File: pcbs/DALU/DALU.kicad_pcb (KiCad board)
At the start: 4 copper layers, 51 parts, among them J201 Conn_02x20_Odd_Even, U201 74HC245, U202 74HC245, U203 74HC245, U301 74HC138, U401 74HC86, U402 74HC86, U403 74HC86, U404 74HC08, U405 74HC283, U406 74HC283, U407 74HC245, U408 74HC245, U501 74HC00, U502 74HC00, U503 74HC245, U601 74HC86, U602 74HC86, U603 74HC245, U701 74HC32, U702 74HC32, U703 74HC245, U801 74HC74, U802 74HC32, U803 74HCT574, U901 74HC08, U902 74HC08, U903 74HC245

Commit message: Fixing a lot of routing
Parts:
- added C401: 100n, Capacitor_SMD:C_0603_1608Metric, F.Cu at (74.9, 47.0)
- added C402: 100n, Capacitor_SMD:C_0603_1608Metric, F.Cu at (58.4, 72.4)
- added C403: 100n, Capacitor_SMD:C_0603_1608Metric, F.Cu at (90.2, 47.0)
- added C404: 100n, Capacitor_SMD:C_0603_1608Metric, F.Cu at (105.4, 47.0)
- added C405: 100n, Capacitor_SMD:C_0603_1608Metric, F.Cu at (73.7, 69.4)
- added C406: 100n, Capacitor_SMD:C_0603_1608Metric, F.Cu at (88.9, 69.3)
- added C501: 100n, Capacitor_SMD:C_0603_1608Metric, F.Cu at (94.0, 138.7)
- added C502: 100n, Capacitor_SMD:C_0603_1608Metric, F.Cu at (97.3, 163.8)
- added C503: 100n, Capacitor_SMD:C_0603_1608Metric, F.Cu at (111.8, 139.7)
- added C601: 100n, Capacitor_SMD:C_0603_1608Metric, F.Cu at (149.9, 47.0)
- added C602: 100n, Capacitor_SMD:C_0603_1608Metric, F.Cu at (149.9, 68.6)
- added C603: 100n, Capacitor_SMD:C_0603_1608Metric, F.Cu at (163.8, 44.5)
- moved U402 61.4 mm to (52.1, 76.2)
- moved U407 23.4 mm to (101.6, 73.7)
- moved U408 16.1 mm to (101.6, 88.9)
- moved U603 4.02 mm to (158.8, 53.3)
- moved U503 4.02 mm to (106.7, 148.6)
- moved U404 1.28 mm to (94.0, 47.0)
- moved U401 1.26 mm to (63.5, 47.0)
- moved U405 1.26 mm to (63.5, 68.6)
- moved C701 0.76 mm to (168.9, 138.7)
- moved C702 0.76 mm to (172.2, 163.8)
- moved C703 0.76 mm to (186.7, 139.7)
- moved U701 0.76 mm to (161.3, 142.2)
- moved U702 0.76 mm to (161.3, 163.8)
- moved U703 0.76 mm to (181.6, 148.6)
- renumbered U404 to U402, U402 to U404
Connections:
- U402 pad 10: unconnected-(U404-Pad10) -> +5V
- U402 pad 11: unconnected-(U404-Pad11) (its old number) -> Net-(U401-Pad10)
- U402 pad 12: unconnected-(U404-Pad12) (its old number) -> /AdderSubtractor/~{ADD}
- U402 pad 13: unconnected-(U404-Pad13) (its old number) -> +5V
- U402 pad 14: unconnected-(U404-Pad14) -> +5V
- U402 pad 7: unconnected-(U404-Pad7) -> GND
- U402 pad 8: unconnected-(U404-Pad8) -> Net-(U403-Pad10)
- U402 pad 9: unconnected-(U404-Pad9) -> /AdderSubtractor/~{ADD}
- U403 pad 10: Net-(U402-Pad6) -> Net-(U403-Pad10)
- U403 pad 13: Net-(U402-Pad6) -> Net-(U403-Pad10)
- U403 pad 2: Net-(U402-Pad6) -> Net-(U403-Pad10)
- U403 pad 5: Net-(U402-Pad6) -> Net-(U403-Pad10)
- U404 pad 1: /AdderSubtractor/~{ADD} -> unconnected-(U404-Pad1)
- U404 pad 10: /AdderSubtractor/~{ADD} -> unconnected-(U404-Pad10)
- U404 pad 2: GND -> unconnected-(U404-Pad2)
- U404 pad 3: Net-(U401-Pad10) -> unconnected-(U404-Pad3)
- U404 pad 5: GND -> Net-(U404-Pad5)
- U404 pad 6: Net-(U402-Pad6) -> Net-(U408-Pad2)
- U404 pad 8: Net-(U402-Pad8) -> unconnected-(U404-Pad8)
- U404 pad 9: Net-(U402-Pad9) -> unconnected-(U404-Pad9)
- U406 pad 9: Net-(U402-Pad9) -> Net-(U404-Pad5)
- U408 pad 2: Net-(U402-Pad8) -> Net-(U408-Pad2)
- U501 pad 1: /AND/A0 -> /AND/A2
- U501 pad 10: /AND/B2 -> /AND/B0
- U501 pad 11: /NAND/NAND3 -> /NAND/NAND1
- U501 pad 12: /AND/A3 -> /AND/A1
- U501 pad 13: /AND/B3 -> /AND/B1
- U501 pad 2: /AND/B0 -> /AND/B2
- U501 pad 3: /NAND/NAND0 -> /NAND/NAND2
- U501 pad 4: /AND/A1 -> /AND/A3
- U501 pad 5: /AND/B1 -> /AND/B3
- U501 pad 6: /NAND/NAND1 -> /NAND/NAND3
- U501 pad 8: /NAND/NAND2 -> /NAND/NAND0
- U501 pad 9: /AND/A2 -> /AND/A0
- U601 pad 1: /AND/A0 -> /AND/A2
- U601 pad 10: /AND/B2 -> /AND/B0
- U601 pad 11: /XOR/XOR3 -> /XOR/XOR1
- U601 pad 12: /AND/A3 -> /AND/A1
- U601 pad 13: /AND/B3 -> /AND/B1
- U601 pad 2: /AND/B0 -> /AND/B2
- U601 pad 3: /XOR/XOR0 -> /XOR/XOR2
- U601 pad 4: /AND/A1 -> /AND/A3
- U601 pad 5: /AND/B1 -> /AND/B3
- U601 pad 6: /XOR/XOR1 -> /XOR/XOR3
- U601 pad 8: /XOR/XOR2 -> /XOR/XOR0
- U601 pad 9: /AND/A2 -> /AND/A0
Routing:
- net /AdderSubtractor/~{OE}: track 0.00 -> 95.4 mm, vias 0 -> 2
- net /AdderSubtractor/~{ADD}: track 0.00 -> 79.4 mm
- net Net-(U403-Pad10): track 0.00 -> 74.6 mm
- net Net-(U404-Pad5): track 0.00 -> 45.7 mm
- net /AdderSubtractor/S_{3}: track 12.6 -> 51.1 mm
- net /AdderSubtractor/S_{0}: track 17.1 -> 54.4 mm
- net Net-(U401-Pad10): track 25.6 -> 55.8 mm
- net Net-(U408-Pad2): track 0.00 -> 29.4 mm, vias 0 -> 1
- net Net-(U402-Pad6): track 25.6 -> 0.00 mm
- net /AdderSubtractor/S_{2}: track 19.7 -> 43.2 mm
- net /AdderSubtractor/S_{1}: track 25.8 -> 46.0 mm
- net /AdderSubtractor/S_{4}: track 22.2 -> 40.2 mm
- net /AdderSubtractor/S_{6}: track 25.3 -> 11.0 mm
- net Net-(U405-Pad9): track 0.00 -> 9.85 mm
- net /XOR/XOR0: track 34.3 -> 26.5 mm
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
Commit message: Routing, routing, routing
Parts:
- added C901: 100n, Capacitor_SMD:C_0603_1608Metric, F.Cu at (125.7, 139.7)
- added C902: 100n, Capacitor_SMD:C_0603_1608Metric, F.Cu at (129.5, 156.2)
- added C903: 100n, Capacitor_SMD:C_0603_1608Metric, F.Cu at (144.8, 139.7)
- moved U803 143.0 mm to (203.2, 110.5)
- moved RN801 141.9 mm to (192.8, 116.1)
- moved RN802 141.9 mm to (194.8, 129.8)
- moved U802 137.2 mm to (198.1, 142.2)
- moved U801 133.4 mm to (210.8, 142.2)
- moved R801 123.6 mm to (224.8, 144.8), turned to -90 degrees
- moved U602 25.2 mm to (119.4, 85.1)
- moved C602 25.2 mm to (130.8, 85.1)
- moved C601 25.2 mm to (130.8, 63.5)
- moved C603 25.2 mm to (144.8, 61.0)
- moved U601 25.2 mm to (119.4, 63.5)
- moved U603 25.2 mm to (139.7, 69.8)
- moved U703 8.89 mm to (172.7, 148.6)
- moved C701 8.89 mm to (160.0, 138.7)
- moved C702 8.89 mm to (163.3, 163.8)
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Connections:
- U901 pad 1: /AND/A0 -> /AND/A2
- U901 pad 10: /AND/B2 -> /AND/B0
- U901 pad 11: /AND/AND3 -> /AND/AND1
- U901 pad 12: /AND/A3 -> /AND/A1
- U901 pad 13: /AND/B3 -> /AND/B1
- U901 pad 14: unconnected-(U901-Pad14) -> +5V
- U901 pad 2: /AND/B0 -> /AND/B2
- U901 pad 3: /AND/AND0 -> /AND/AND2
- U901 pad 4: /AND/A1 -> /AND/A3
- U901 pad 5: /AND/B1 -> /AND/B3
- U901 pad 6: /AND/AND1 -> /AND/AND3
- U901 pad 7: unconnected-(U901-Pad7) -> GND
- U901 pad 8: /AND/AND2 -> /AND/AND0
- U901 pad 9: /AND/A2 -> /AND/A0
- U902 pad 14: unconnected-(U902-Pad14) -> +5V
- U902 pad 7: unconnected-(U902-Pad7) -> GND
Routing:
- net /AND/B0: track 188.2 -> 318.5 mm, vias 1 -> 5
- net /AND/B5: track 196.0 -> 323.4 mm, vias 1 -> 4
- net /AND/A3: track 176.5 -> 300.5 mm, vias 1 -> 4
- net /AND/B6: track 213.6 -> 334.2 mm, vias 1 -> 5
- net /AND/B1: track 176.3 -> 296.6 mm, vias 1 -> 5
- net /AND/B7: track 209.3 -> 329.1 mm, vias 1 -> 5
- net /AND/A0: track 179.1 -> 296.2 mm, vias 1 -> 6
- net /AND/A2: track 178.8 -> 294.5 mm, vias 1 -> 4
- net /AND/B3: track 180.8 -> 293.4 mm, vias 1 -> 5
- net /AND/A1: track 180.6 -> 290.1 mm, vias 1 -> 6
- net /AND/B4: track 213.4 -> 322.5 mm, vias 1 -> 4
- net /AND/B2: track 168.4 -> 275.8 mm, vias 1 -> 5
- net /AND/A5: track 218.9 -> 324.3 mm, vias 1 -> 5
- net /AND/A7: track 208.3 -> 313.4 mm, vias 1 -> 5
- net /AND/A4: track 200.6 -> 304.0 mm, vias 1 -> 5
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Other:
- board text removed: "Result bus goes here"

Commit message: More rerouting
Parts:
- moved U801 73.7 mm to (167.6, 82.5)
- moved U802 73.7 mm to (154.9, 82.5)
- moved R801 73.7 mm to (181.6, 85.1)
- moved RN801 26.3 mm to (188.0, 90.2)
- moved RN802 21.8 mm to (190.5, 151.1)
- moved U803 20.7 mm to (182.9, 106.7)
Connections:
- RN801 pad 5: Net-(RN801-Pad5) -> /AND/RESULT3
- RN801 pad 6: Net-(RN801-Pad6) -> /AND/RESULT2
- RN801 pad 7: Net-(RN801-Pad7) -> /AND/RESULT1
- RN801 pad 8: Net-(RN801-Pad8) -> /AND/RESULT0
- RN802 pad 5: Net-(RN802-Pad5) -> /AND/RESULT7
- RN802 pad 6: Net-(RN802-Pad6) -> /AND/RESULT6
- RN802 pad 7: Net-(RN802-Pad7) -> /AND/RESULT5
- RN802 pad 8: Net-(RN802-Pad8) -> /AND/RESULT4
- U407 pad 11: unconnected-(U407-Pad11) -> /AND/RESULT7
- U407 pad 12: unconnected-(U407-Pad12) -> /AND/RESULT6
- U407 pad 13: unconnected-(U407-Pad13) -> /AND/RESULT5
- U407 pad 14: unconnected-(U407-Pad14) -> /AND/RESULT4
- U407 pad 15: unconnected-(U407-Pad15) -> /AND/RESULT3
- U407 pad 16: unconnected-(U407-Pad16) -> /AND/RESULT2
- U407 pad 17: unconnected-(U407-Pad17) -> /AND/RESULT1
- U407 pad 18: unconnected-(U407-Pad18) -> /AND/RESULT0
- U503 pad 11: /NAND/RESULT7 -> /AND/RESULT7
- U503 pad 12: /NAND/RESULT6 -> /AND/RESULT6
- U503 pad 13: /NAND/RESULT5 -> /AND/RESULT5
- U503 pad 14: /NAND/RESULT4 -> /AND/RESULT4
- U503 pad 15: /NAND/RESULT3 -> /AND/RESULT3
- U503 pad 16: /NAND/RESULT2 -> /AND/RESULT2
- U503 pad 17: /NAND/RESULT1 -> /AND/RESULT1
- U503 pad 18: /NAND/RESULT0 -> /AND/RESULT0
- U603 pad 11: unconnected-(U603-Pad11) -> /AND/RESULT7
- U603 pad 12: unconnected-(U603-Pad12) -> /AND/RESULT6
- U603 pad 13: unconnected-(U603-Pad13) -> /AND/RESULT5
- U603 pad 14: unconnected-(U603-Pad14) -> /AND/RESULT4
- U603 pad 15: unconnected-(U603-Pad15) -> /AND/RESULT3
- U603 pad 16: unconnected-(U603-Pad16) -> /AND/RESULT2
- U603 pad 17: unconnected-(U603-Pad17) -> /AND/RESULT1
- U603 pad 18: unconnected-(U603-Pad18) -> /AND/RESULT0
- U703 pad 11: unconnected-(U703-Pad11) -> /AND/RESULT7
- U703 pad 12: unconnected-(U703-Pad12) -> /AND/RESULT6
- U703 pad 13: unconnected-(U703-Pad13) -> /AND/RESULT5
- U703 pad 14: unconnected-(U703-Pad14) -> /AND/RESULT4
- U703 pad 15: unconnected-(U703-Pad15) -> /AND/RESULT3
- U703 pad 16: unconnected-(U703-Pad16) -> /AND/RESULT2
- U703 pad 17: unconnected-(U703-Pad17) -> /AND/RESULT1
- U703 pad 18: unconnected-(U703-Pad18) -> /AND/RESULT0
- U803 pad 2: Net-(RN801-Pad8) -> /AND/RESULT0
- U803 pad 3: Net-(RN801-Pad7) -> /AND/RESULT1
- U803 pad 4: Net-(RN801-Pad6) -> /AND/RESULT2
- U803 pad 5: Net-(RN801-Pad5) -> /AND/RESULT3
- U803 pad 6: Net-(RN802-Pad8) -> /AND/RESULT4
- U803 pad 7: Net-(RN802-Pad7) -> /AND/RESULT5
- U803 pad 8: Net-(RN802-Pad6) -> /AND/RESULT6
- U803 pad 9: Net-(RN802-Pad5) -> /AND/RESULT7
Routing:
- net /AND/RESULT7: track 0.00 -> 290.3 mm, vias 0 -> 8
- net /AND/RESULT6: track 0.00 -> 285.2 mm, vias 0 -> 8
- net /AND/RESULT5: track 0.00 -> 280.2 mm, vias 0 -> 8
- net /AND/RESULT4: track 0.00 -> 275.1 mm, vias 0 -> 8
- net /AND/RESULT3: track 0.00 -> 270.0 mm, vias 0 -> 8
- net /AND/RESULT2: track 0.00 -> 264.9 mm, vias 0 -> 8
- net /AND/RESULT1: track 0.00 -> 259.8 mm, vias 0 -> 8
- net /AND/RESULT0: track 0.00 -> 255.0 mm, vias 0 -> 8
- net /NAND/RESULT7: track 39.2 -> 0.00 mm, vias 2 -> 0
- net /NAND/RESULT6: track 38.0 -> 0.00 mm, vias 2 -> 0
- net /NAND/RESULT5: track 36.7 -> 0.00 mm, vias 2 -> 0
- net /NAND/RESULT4: track 35.4 -> 0.00 mm, vias 2 -> 0
- net /NAND/RESULT3: track 34.2 -> 0.00 mm, vias 2 -> 0
- net /NAND/RESULT2: track 32.9 -> 0.00 mm, vias 2 -> 0
- net /NAND/RESULT1: track 31.6 -> 0.00 mm, vias 2 -> 0
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
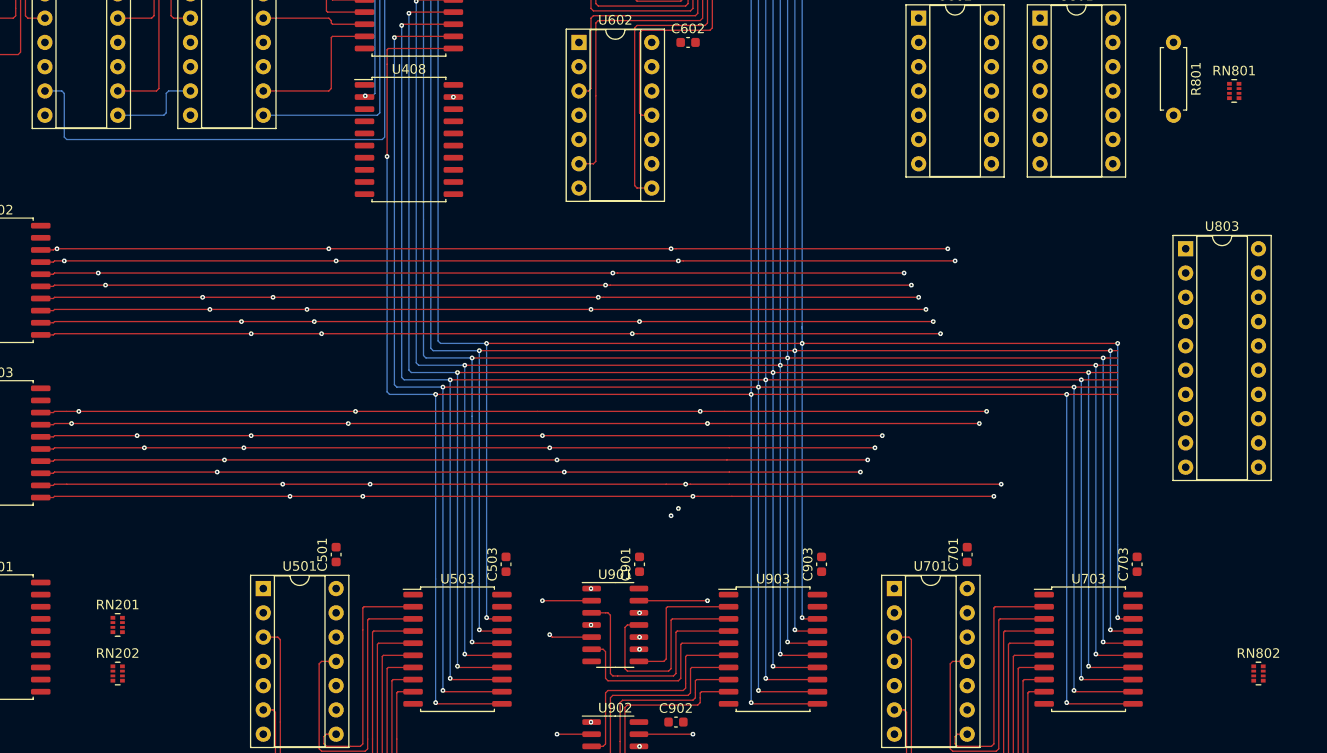
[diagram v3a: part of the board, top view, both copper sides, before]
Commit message: Redoing resistors
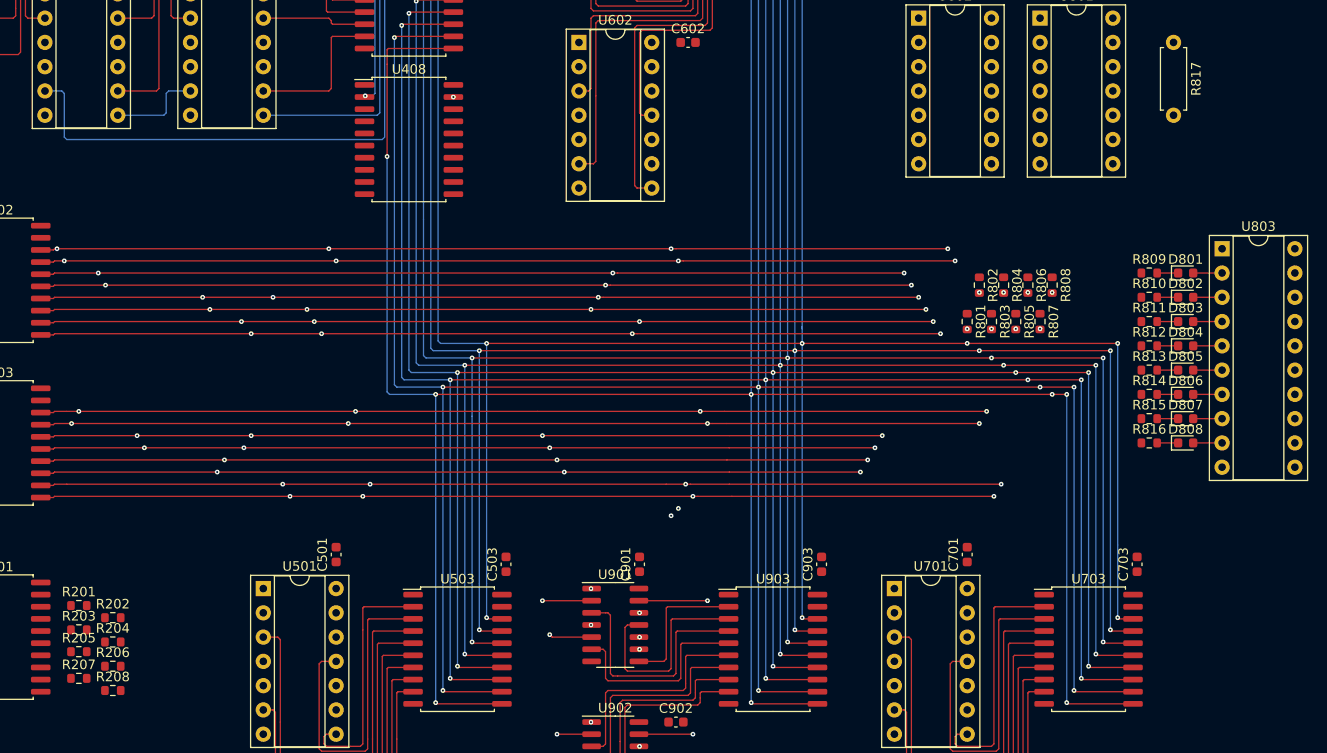
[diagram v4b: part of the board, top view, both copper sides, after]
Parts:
- removed RN201, RN202, RN801, RN802: 10k, Resistor_SMD:R_Array_Convex_4x0402
- added D801: LED, LED_SMD:LED_0603_1608Metric, F.Cu at (182.9, 109.2)
- added D802: LED, LED_SMD:LED_0603_1608Metric, F.Cu at (182.9, 111.8)
- added D803: LED, LED_SMD:LED_0603_1608Metric, F.Cu at (182.9, 114.3)
- added D804: LED, LED_SMD:LED_0603_1608Metric, F.Cu at (182.9, 116.8)
- added D805: LED, LED_SMD:LED_0603_1608Metric, F.Cu at (182.9, 119.4)
- added D806: LED, LED_SMD:LED_0603_1608Metric, F.Cu at (182.9, 121.9)
- added D807: LED, LED_SMD:LED_0603_1608Metric, F.Cu at (182.9, 124.5)
- added D808: LED, LED_SMD:LED_0603_1608Metric, F.Cu at (182.9, 127.0)
- added R201: 220k, Resistor_SMD:R_0603_1608Metric, F.Cu at (67.1, 144.0)
- added R202: 220k, Resistor_SMD:R_0603_1608Metric, F.Cu at (70.6, 145.3)
- added R203: 220k, Resistor_SMD:R_0603_1608Metric, F.Cu at (67.1, 146.6)
- added R204: 220k, Resistor_SMD:R_0603_1608Metric, F.Cu at (70.6, 147.8)
- added R205: 220k, Resistor_SMD:R_0603_1608Metric, F.Cu at (67.1, 148.8)
- added R206: 220k, Resistor_SMD:R_0603_1608Metric, F.Cu at (70.6, 150.4)
- added R207: 220k, Resistor_SMD:R_0603_1608Metric, F.Cu at (67.1, 151.6)
- added R208: 220k, Resistor_SMD:R_0603_1608Metric, F.Cu at (70.6, 152.9)
- added R801: 220k, Resistor_SMD:R_0603_1608Metric, F.Cu at (160.0, 114.3)
- added R802: 220k, Resistor_SMD:R_0603_1608Metric, F.Cu at (161.3, 110.5)
- added R803: 220k, Resistor_SMD:R_0603_1608Metric, F.Cu at (162.6, 114.3)
- added R804: 220k, Resistor_SMD:R_0603_1608Metric, F.Cu at (163.8, 110.5)
- added R805: 220k, Resistor_SMD:R_0603_1608Metric, F.Cu at (165.1, 114.3)
- added R806: 220k, Resistor_SMD:R_0603_1608Metric, F.Cu at (166.4, 110.5)
- added R807: 220k, Resistor_SMD:R_0603_1608Metric, F.Cu at (167.6, 114.3)
- added R808: 220k, Resistor_SMD:R_0603_1608Metric, F.Cu at (168.9, 110.5)
- added R809: 4k7, Resistor_SMD:R_0603_1608Metric, F.Cu at (179.1, 109.2)
- added R810: 4k7, Resistor_SMD:R_0603_1608Metric, F.Cu at (179.1, 111.8)
- added R811: 4k7, Resistor_SMD:R_0603_1608Metric, F.Cu at (179.1, 114.3)
- added R812: 4k7, Resistor_SMD:R_0603_1608Metric, F.Cu at (179.1, 116.8)
- added R813: 4k7, Resistor_SMD:R_0603_1608Metric, F.Cu at (179.1, 119.4)
- added R814: 4k7, Resistor_SMD:R_0603_1608Metric, F.Cu at (179.1, 121.9)
- added R815: 4k7, Resistor_SMD:R_0603_1608Metric, F.Cu at (179.1, 124.5)
- added R816: 4k7, Resistor_SMD:R_0603_1608Metric, F.Cu at (179.1, 127.0)
- moved U803 3.81 mm to (186.7, 106.7)
- renumbered R801 to R817
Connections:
- U803 pad 12: unconnected-(U803-Pad12) -> /Output Stage/C7
- U803 pad 13: unconnected-(U803-Pad13) -> /Output Stage/C6
- U803 pad 14: unconnected-(U803-Pad14) -> /Output Stage/C5
- U803 pad 15: unconnected-(U803-Pad15) -> /Output Stage/C4
- U803 pad 16: unconnected-(U803-Pad16) -> /Output Stage/C3
- U803 pad 17: unconnected-(U803-Pad17) -> /Output Stage/C2
- U803 pad 18: unconnected-(U803-Pad18) -> /Output Stage/C1
- U803 pad 19: unconnected-(U803-Pad19) -> /Output Stage/C0
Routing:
- net /AND/RESULT7: track 290.3 -> 319.7 mm, vias 8 -> 10
- net /AND/RESULT1: track 259.8 -> 285.2 mm, vias 8 -> 10
- net /AND/RESULT5: track 280.2 -> 304.5 mm, vias 8 -> 10
- net /AND/RESULT3: track 270.0 -> 293.3 mm, vias 8 -> 10
- net /AND/RESULT6: track 285.2 -> 308.3 mm, vias 8 -> 10
- net /AND/RESULT0: track 255.0 -> 277.5 mm, vias 8 -> 10
- net /AND/RESULT2: track 264.9 -> 285.4 mm, vias 8 -> 10
- net /AND/RESULT4: track 275.1 -> 293.7 mm, vias 8 -> 10
- net Net-(R816-Pad2): track 0.00 -> 2.20 mm
- net Net-(R815-Pad2): track 0.00 -> 2.20 mm
- net Net-(R811-Pad2): track 0.00 -> 2.20 mm
- net Net-(D806-Pad1): track 0.00 -> 2.20 mm
- net Net-(D805-Pad1): track 0.00 -> 2.20 mm
- net Net-(D804-Pad1): track 0.00 -> 2.20 mm
- net Net-(D802-Pad1): track 0.00 -> 2.20 mm
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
